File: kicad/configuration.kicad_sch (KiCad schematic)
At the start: 34 parts, among them J3 USB C, J4 HIC SWD, U1 MIMXRT1171DVMAB, U6 W25Q64JWUUIQ, U7 MKL26Z128VFM4, Y2 16MHz

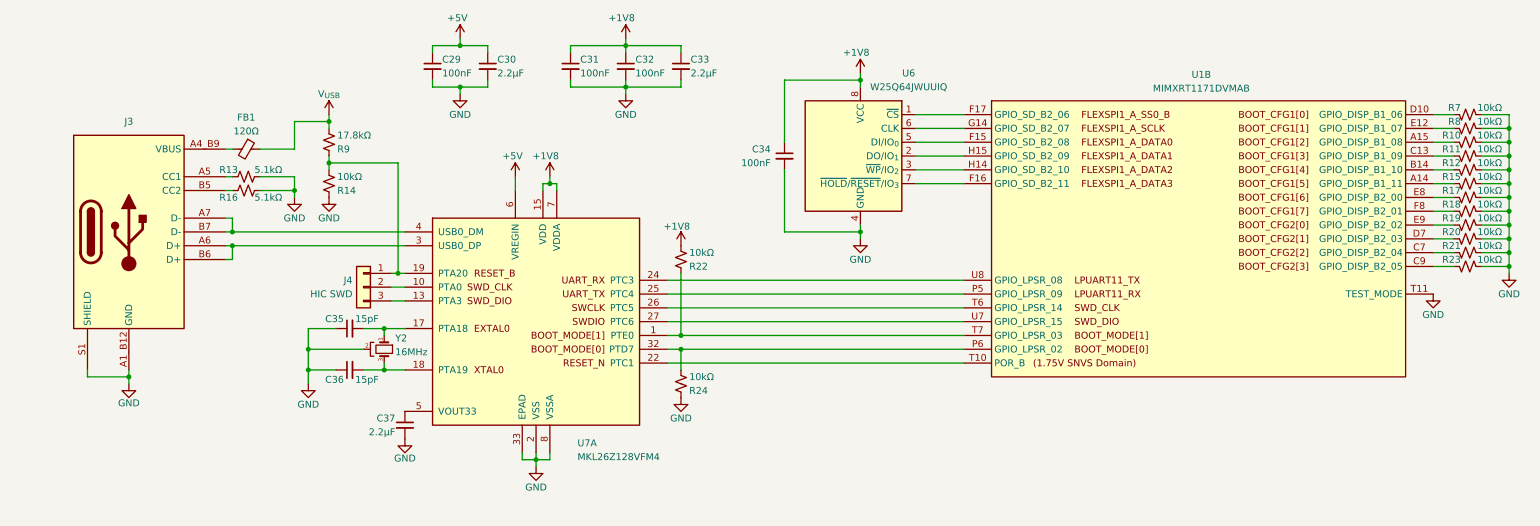
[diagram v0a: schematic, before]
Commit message: added pull-up resistors to W25Q QSPI line
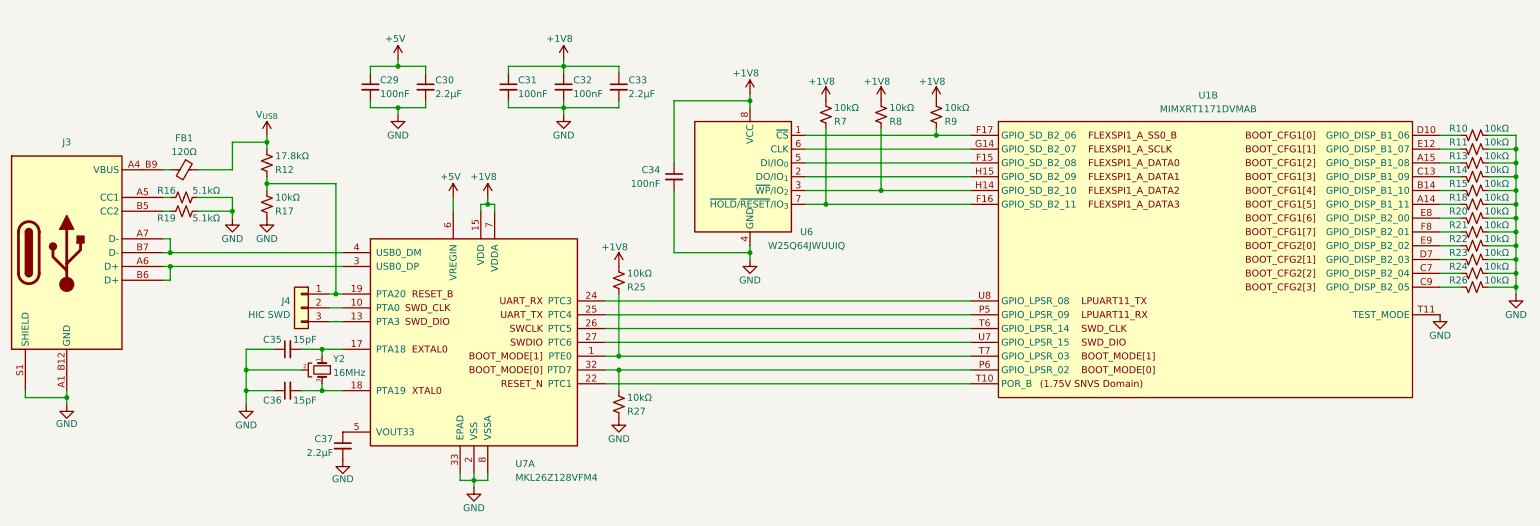
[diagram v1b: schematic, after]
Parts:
- added R7, R8, R9: 10kΩ, Resistor_SMD:R_0201_0603Metric, symbol Device:R_Small_US
- renumbered R7 to R10, R8 to R11, R9 to R12, R10 to R13, R11 to R14, R12 to R15, R13 to R16, R14 to R17, R15 to R18, R16 to R19, R17 to R20, R18 to R21, R19 to R22, R20 to R23, R21 to R24, R22 to R25, R23 to R26, R24 to R27
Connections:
- net +1V8: now also R7.2, R8.2, R9.2
- net at U1.F17 (GPIO_SD_B2_06), U6.1 (~{CS}): now also R9.1
- net at U1.H14 (GPIO_SD_B2_10), U6.3 (~{WP}/IO_{2}): now also R8.1
- net at U1.F16 (GPIO_SD_B2_11), U6.7 (~{HOLD}/~{RESET}/IO_{3}): now also R7.1
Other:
- moved on the sheet: C29, C30, C31, C32, C33, C34, C35, C36, C37, FB1, J3, J4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
